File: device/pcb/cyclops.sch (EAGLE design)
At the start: 184 parts, among them Q1 NDS351AN, Q2 NDS351AN, Q3 NDS351AN, Q4 IRF510, U1 MCP4921, U10 ADG1201, U11 THS4281, U12 MAX4564, U13 ZXTD, U14 ZXTD, U15 OPA1664, U16 LTM8020, U2 LT1931, U3 LT1764A, U4 BD00FC0WEFJ, U5 TPS72325, U6 LT1711, U7 TLV3701, U8 ADR03, U9 LT1880

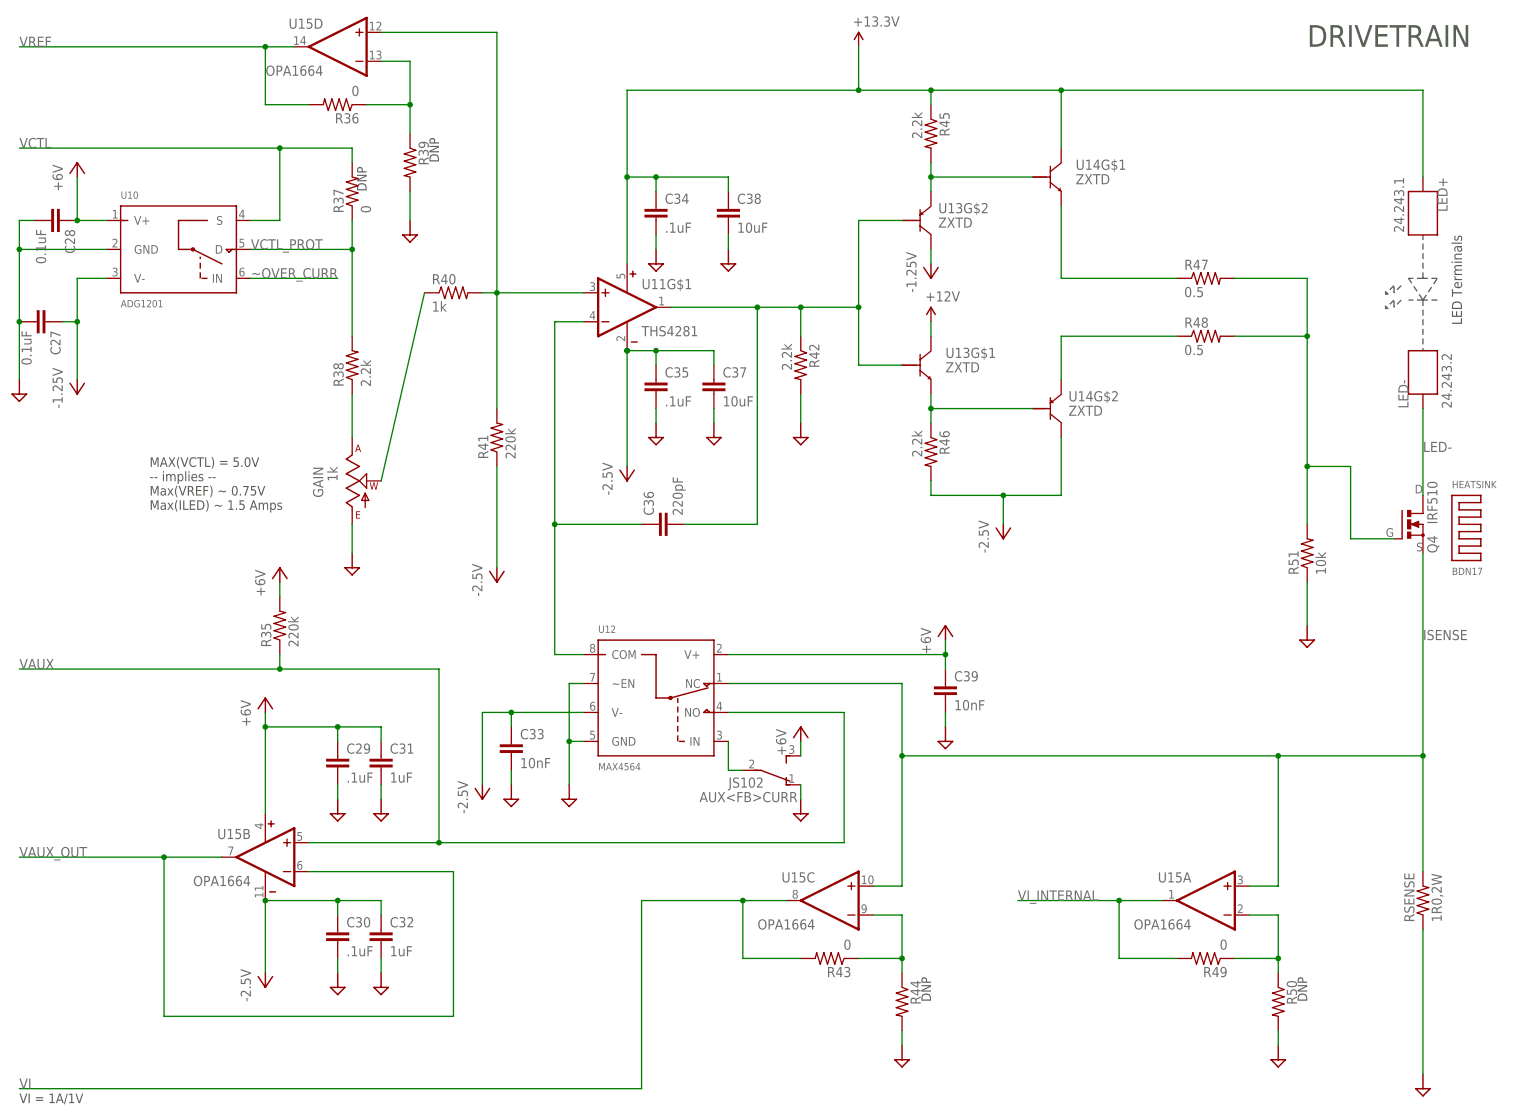
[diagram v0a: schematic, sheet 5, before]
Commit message: Stablized booster stage for high side LED.
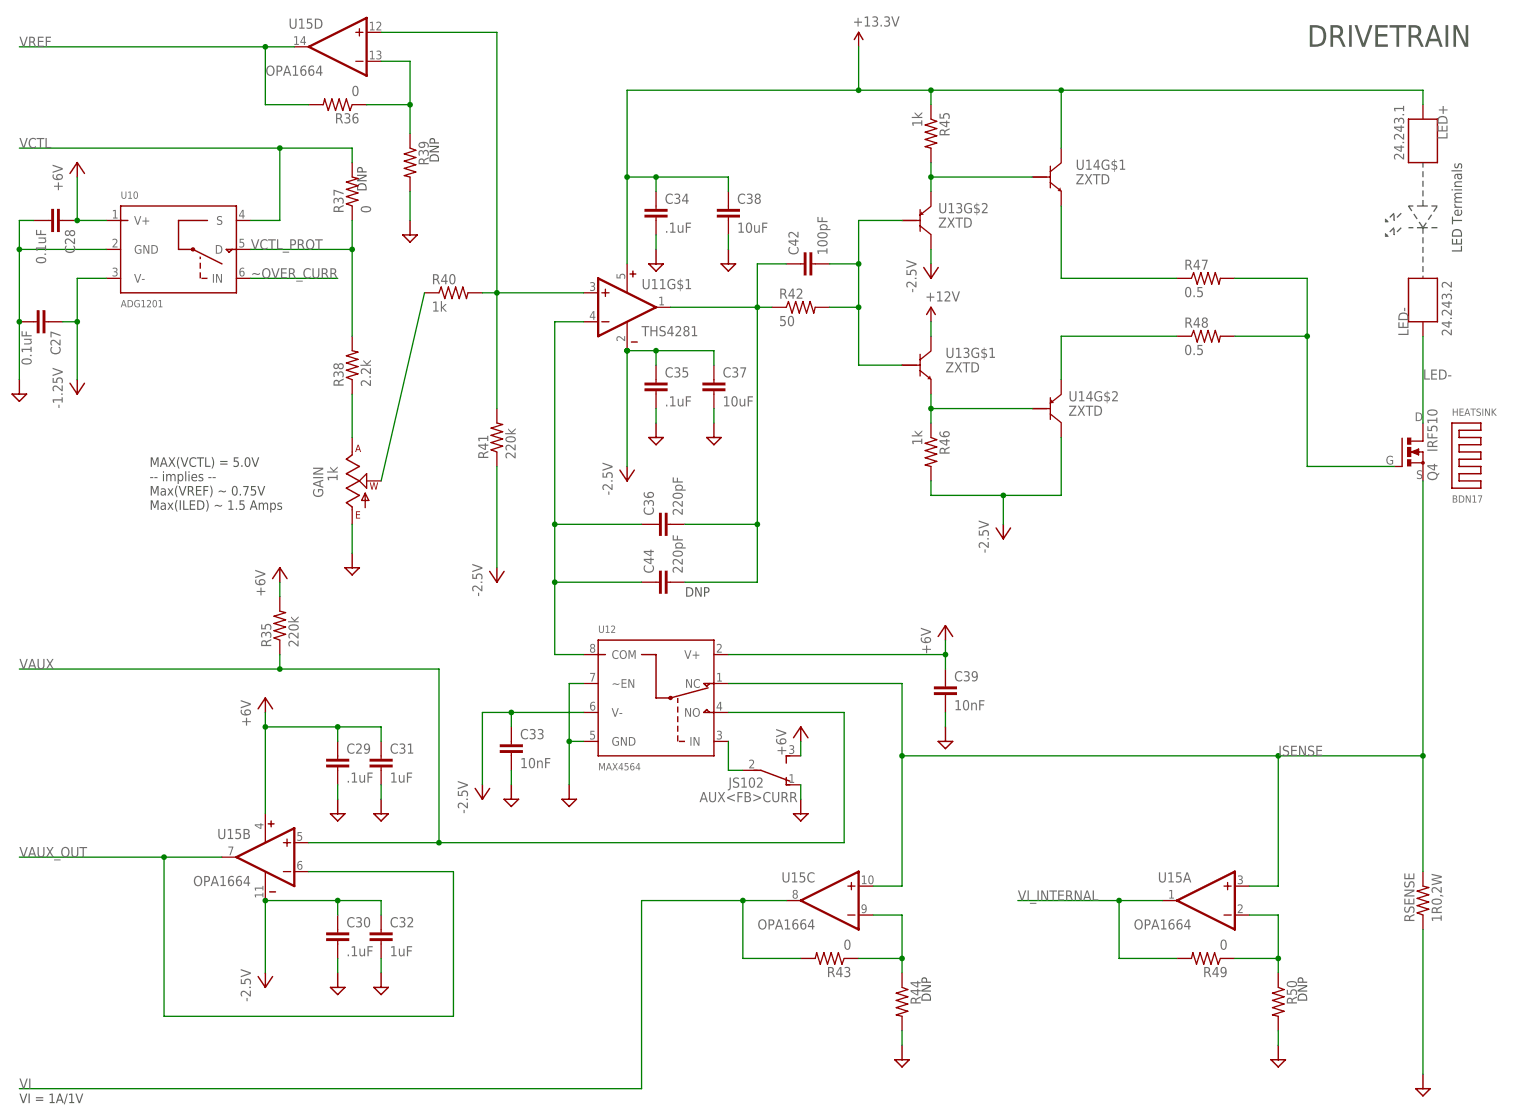
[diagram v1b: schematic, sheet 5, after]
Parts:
- removed R51: 10k, cyclops:R_0603
- added C42: 100pF, cyclops:C_0603
- added C44: 220pF, cyclops:C_0603
- R42: value 2.2k -> 50
- R45, R46: value 2.2k -> 1k
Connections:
- new net N$16: C42.2, R42.2, U13G$1.B, U13G$2.B
- net COM: now also C44.1
- net GND: no longer R42.2, R51.1
- net N$13: now also C42.1, C44.2; no longer U13G$1.B, U13G$2.B
- net N$26: no longer R51.2
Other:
- moved on the sheet: HEATSINK, LED+, LED-, Q4, R42

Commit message: Final circuit changes before production.
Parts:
- removed C26: .1uF, cyclops:C_0603
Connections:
- net GND: no longer C26.2
- net REF5.0: no longer C26.1
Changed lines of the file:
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@@
 <?xml version="1.0" encoding="utf-8"?>
 <!DOCTYPE eagle SYSTEM "eagle.dtd">
-<eagle version="6.6.0">
+<eagle version="6.5.0">
 <drawing>
 <settings>
@@
 <setting verticaltext="up"/>
 </settings>
-<grid distance="0.1" unitdist="inch" unit="inch" style="lines" multiple="1" display="yes" altdistance="0.01" altunitdist="inch" altunit="inch"/>
+<grid distance="0.1" unitdist="inch" unit="inch" style="lines" multiple="1" display="no" altdistance="0.01" altunitdist="inch" altunit="inch"/>
 <layers>
 <layer number="1" name="Top" color="4" fill="1" visible="no" active="no"/>
@@
 <part name="R33" library="cyclops" deviceset="R" device="_0603" value="1k"/>
 <part name="R34" library="cyclops" deviceset="R" device="_0603" value="1k"/>
-<part name="C26" library="cyclops" deviceset="C" device="_0603" value=".1uF"/>
 <part name="U$44" library="cyclops" deviceset="GND2" device=""/>
-<part name="U$46" library="cyclops" deviceset="GND2" device=""/>
 <part name="HEATSINK" library="jonnew" deviceset="HEATSINK" device="_BDN17" value="BDN17"/>
 <part name="R36" library="cyclops" deviceset="R" device="_0603" value="0"/>
@@
 <instance part="R33" gate="R" x="-15.24" y="-55.88" rot="R270"/>
 <instance part="R34" gate="R" x="5.08" y="-45.72" rot="R180"/>
-<instance part="C26" gate="C" x="53.34" y="-27.94"/>
 <instance part="U$44" gate="G$1" x="-15.24" y="-76.2"/>
-<instance part="U$46" gate="G$1" x="53.34" y="-76.2"/>
 <instance part="P+16" gate="1" x="25.4" y="15.24" rot="MR0"/>
 <instance part="P+17" gate="1" x="-139.7" y="-10.16"/>
@@
 </segment>
 <segment>
-<pinref part="C26" gate="C" pin="2"/>
-<wire x1="53.34" y1="-33.02" x2="53.34" y2="-73.66" width="0.1524" layer="91"/>
-</segment>
-<segment>
 <pinref part="U9" gate="G$2" pin="V-"/>
 <wire x1="5.08" y1="-35.56" x2="5.08" y2="-27.94" width="0.1524" layer="91"/>
@@
 <wire x1="22.86" y1="-45.72" x2="22.86" y2="-20.32" width="0.1524" layer="91"/>
 <junction x="22.86" y="-20.32"/>
-<pinref part="C26" gate="C" pin="1"/>
-<wire x1="53.34" y1="-20.32" x2="53.34" y2="-25.4" width="0.1524" layer="91"/>
 <wire x1="53.34" y1="-20.32" x2="83.82" y2="-20.32" width="0.1524" layer="91"/>
 <junction x="53.34" y="-20.32"/>
